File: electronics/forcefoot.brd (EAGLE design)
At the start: 60 x 43.6 mm, 71 parts, among them U2 ATMEGA168

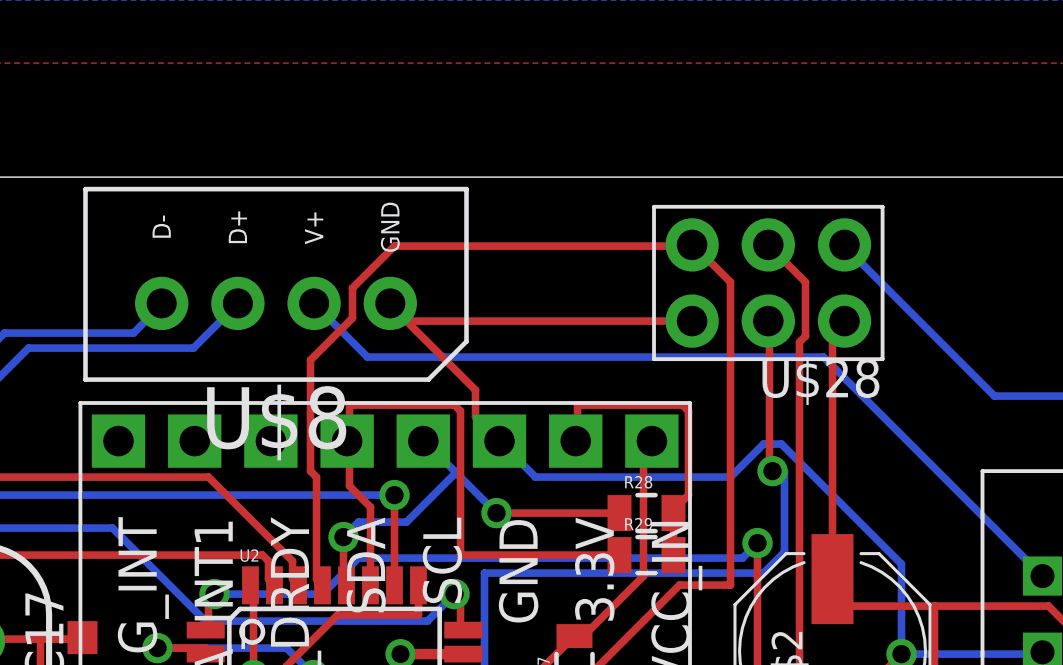
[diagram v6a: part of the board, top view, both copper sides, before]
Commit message: Improving names and silk
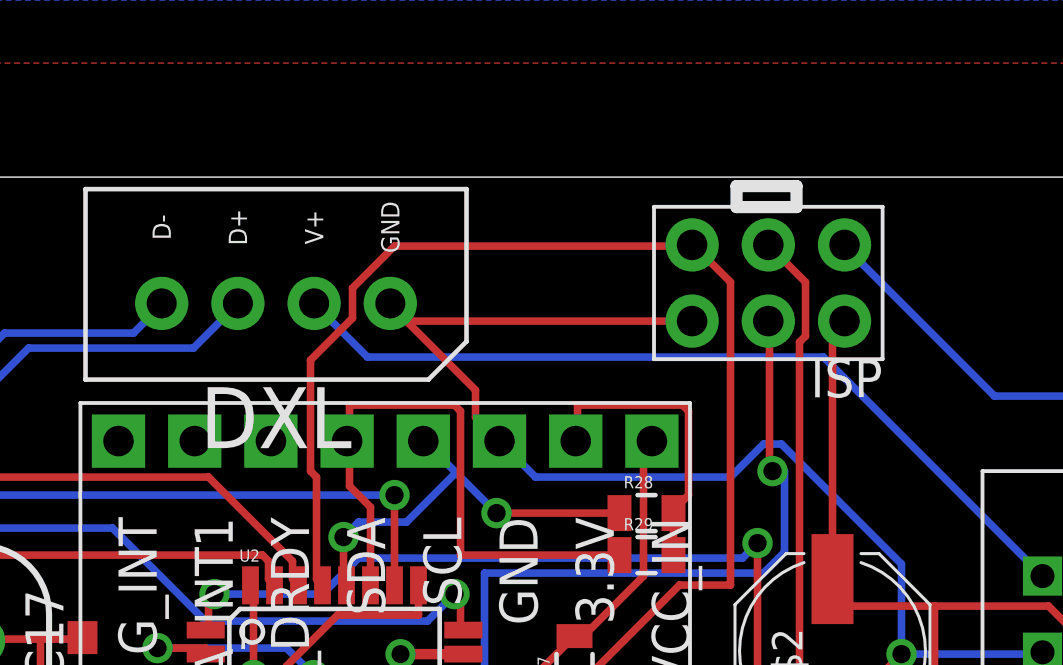
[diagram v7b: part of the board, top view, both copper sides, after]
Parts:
- renumbered U$17 to IMU, U$28 to ISP, U$5 to REG, U$8 to DXL
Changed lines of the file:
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@@
 <rectangle x1="25.912528125" y1="-0.308484375" x2="32.559784375" y2="6.769321875" layer="41"/>
 <rectangle x1="25.8976" y1="-0.31628125" x2="32.5570125" y2="6.77680625" layer="42"/>
+<wire x1="43.6" y1="42.4" x2="43.6" y2="43.1" width="0.4064" layer="25"/>
+<wire x1="43.6" y1="43.1" x2="45.6" y2="43.1" width="0.4064" layer="25"/>
+<wire x1="45.6" y1="43.1" x2="45.6" y2="42.4" width="0.4064" layer="25"/>
+<wire x1="45.6" y1="42.4" x2="43.6" y2="42.4" width="0.4064" layer="25"/>
 </plain>
 <attributes>
@@
 <element name="C18" library="rhoban" package="C0603" value="22" x="21.8" y="23.8" rot="R270"/>
 <element name="R27" library="SparkFun-Passives" package="0805" value="10k" x="38.2" y="27.2" rot="R90"/>
-<element name="U$28" library="rhoban" package="CONNEC_2X03" value="CONNEC_2X03" x="47.2" y="38.6" rot="R180"/>
-<element name="U$5" library="rhoban" package="TRACOPOWER" value="REG_5V" x="51.8" y="33.6" rot="R270"/>
-<element name="U$8" library="rhoban" package="CONNEC_485" value="CONNEC_1X04_485" x="34.6" y="43" rot="R180"/>
+<element name="ISP" library="rhoban" package="CONNEC_2X03" value="CONNEC_2X03" x="47.2" y="38.6" rot="R180"/>
+<element name="REG" library="rhoban" package="TRACOPOWER" value="REG_5V" x="51.8" y="33.6" rot="R270"/>
+<element name="DXL" library="rhoban" package="CONNEC_485" value="CONNEC_1X04_485" x="34.6" y="43" rot="R180"/>
 <element name="U$11" library="SparkFun-Electromechanical" package="STAND-OFF" value="" x="3.29684375" y="40.111128125"/>
 <element name="U$14" library="SparkFun-Electromechanical" package="STAND-OFF" value="" x="56.49684375" y="39.711128125"/>
 <element name="U$16" library="SparkFun-Electromechanical" package="STAND-OFF" value="" x="29.09684375" y="3.111128125"/>
-<element name="U$17" library="rhoban" package="GY-85" value="GY-85" x="23" y="34.6" rot="R270"/>
+<element name="IMU" library="rhoban" package="GY-85" value="GY-85" x="23" y="34.6" rot="R270"/>
 <element name="R28" library="SparkFun-Passives" package="0805" value="3K" x="40.6" y="32.2"/>
 <element name="R29" library="SparkFun-Passives" package="0805" value="3K" x="40.6" y="30.8"/>
@@
 <contactref element="C17" pad="1"/>
 <contactref element="C18" pad="1"/>
-<contactref element="U$28" pad="6"/>
-<contactref element="U$5" pad="P$2"/>
-<contactref element="U$8" pad="GND"/>
-<contactref element="U$17" pad="GND"/>
+<contactref element="ISP" pad="6"/>
+<contactref element="REG" pad="P$2"/>
+<contactref element="DXL" pad="GND"/>
+<contactref element="IMU" pad="GND"/>
 <contactref element="HX1" pad="14"/>
 <contactref element="HX1" pad="5"/>
@@
 <contactref element="U$2" pad="+"/>
 <contactref element="U$4" pad="+"/>
-<contactref element="U$5" pad="P$3"/>
-<contactref element="U$17" pad="VCC_IN"/>
+<contactref element="REG" pad="P$3"/>
+<contactref element="IMU" pad="VCC_IN"/>
 <contactref element="HX1" pad="1"/>
 <contactref element="HX1" pad="16"/>
@@
 <contactref element="U2" pad="20"/>
 <contactref element="R27" pad="2"/>
-<contactref element="U$28" pad="2"/>
+<contactref element="ISP" pad="2"/>
 <wire x1="8.7" y1="30.2" x2="5.7" y2="33.2" width="0.254" layer="1"/>
 <wire x1="9.8" y1="30.2" x2="8.7" y2="30.2" width="0.254" layer="1"/>
@@
 </signal>
 <signal name="VIN">
-<contactref element="U$5" pad="P$1"/>
-<contactref element="U$8" pad="V+"/>
+<contactref element="REG" pad="P$1"/>
+<contactref element="DXL" pad="V+"/>
 <wire x1="46.5" y1="37.4" x2="53.8" y2="30.1" width="0.254" layer="16"/>
 <wire x1="31.3" y1="37.4" x2="46.5" y2="37.4" width="0.254" layer="16"/>
@@
 <signal name="RS+">
 <contactref element="R14" pad="1"/>
-<contactref element="U$8" pad="D+"/>
+<contactref element="DXL" pad="D+"/>
 <wire x1="15.2" y1="28.2" x2="14.2" y2="27.2" width="0.254" layer="1"/>
 <wire x1="15.2" y1="32.3" x2="15.2" y2="28.2" width="0.254" layer="1"/>
@@
 <contactref element="R2" pad="1"/>
 <contactref element="R15" pad="1"/>
-<contactref element="U$8" pad="D-"/>
+<contactref element="DXL" pad="D-"/>
 <wire x1="10.05" y1="33.2" x2="7.55" y2="33.2" width="0.254" layer="1"/>
 <wire x1="11.4" y1="32.1" x2="12.25" y2="31.25" width="0.254" layer="1"/>
@@
 <signal name="RESET">
 <contactref element="R27" pad="1"/>
-<contactref element="U$28" pad="5"/>
+<contactref element="ISP" pad="5"/>
 <contactref element="U2" pad="29"/>
 <wire x1="41.7" y1="29.8" x2="38.2" y2="26.3" width="0.254" layer="1"/>
@@
 </signal>
 <signal name="SCK">
-<contactref element="U$28" pad="3"/>
+<contactref element="ISP" pad="3"/>
 <contactref element="U2" pad="17"/>
 <wire x1="34.8" y1="22.4" x2="34.5" y2="22.7" width="0.254" layer="1"/>
@@
 </signal>
 <signal name="MOSI">
-<contactref element="U$28" pad="4"/>
+<contactref element="ISP" pad="4"/>
 <contactref element="U2" pad="15"/>
 <wire x1="32.1" y1="21.1" x2="32.2" y2="21.2" width="0.254" layer="1"/>
@@
 </signal>
 <signal name="MISO">
-<contactref element="U$28" pad="1"/>
+<contactref element="ISP" pad="1"/>
 <contactref element="U2" pad="16"/>
 <wire x1="33.3" y1="20.9" x2="33" y2="21.2" width="0.254" layer="1"/>
@@
 </signal>
 <signal name="IMU_SCL">
-<contactref element="U$17" pad="SCL"/>
+<contactref element="IMU" pad="SCL"/>
 <contactref element="R28" pad="1"/>
 <contactref element="U2" pad="28"/>
@@
 </signal>
 <signal name="IMU_SDA">
-<contactref element="U$17" pad="SDA"/>
+<contactref element="IMU" pad="SDA"/>
 <contactref element="R29" pad="1"/>
 <contactref element="U2" pad="27"/>
@@
 </signal>
 <signal name="3.3">
-<contactref element="U$17" pad="3.3"/>
+<contactref element="IMU" pad="3.3"/>
 <contactref element="R29" pad="2"/>
 <contactref element="R28" pad="2"/>
